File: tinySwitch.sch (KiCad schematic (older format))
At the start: 14 parts, among them J0 Conn_01x02, J1 Conn_01x03, J2 Conn_01x02, J3 Conn_01x02, J4 Conn_01x02, K1 1 Channel Relay, SW1 Power Button, U1 Digispark Tiny85

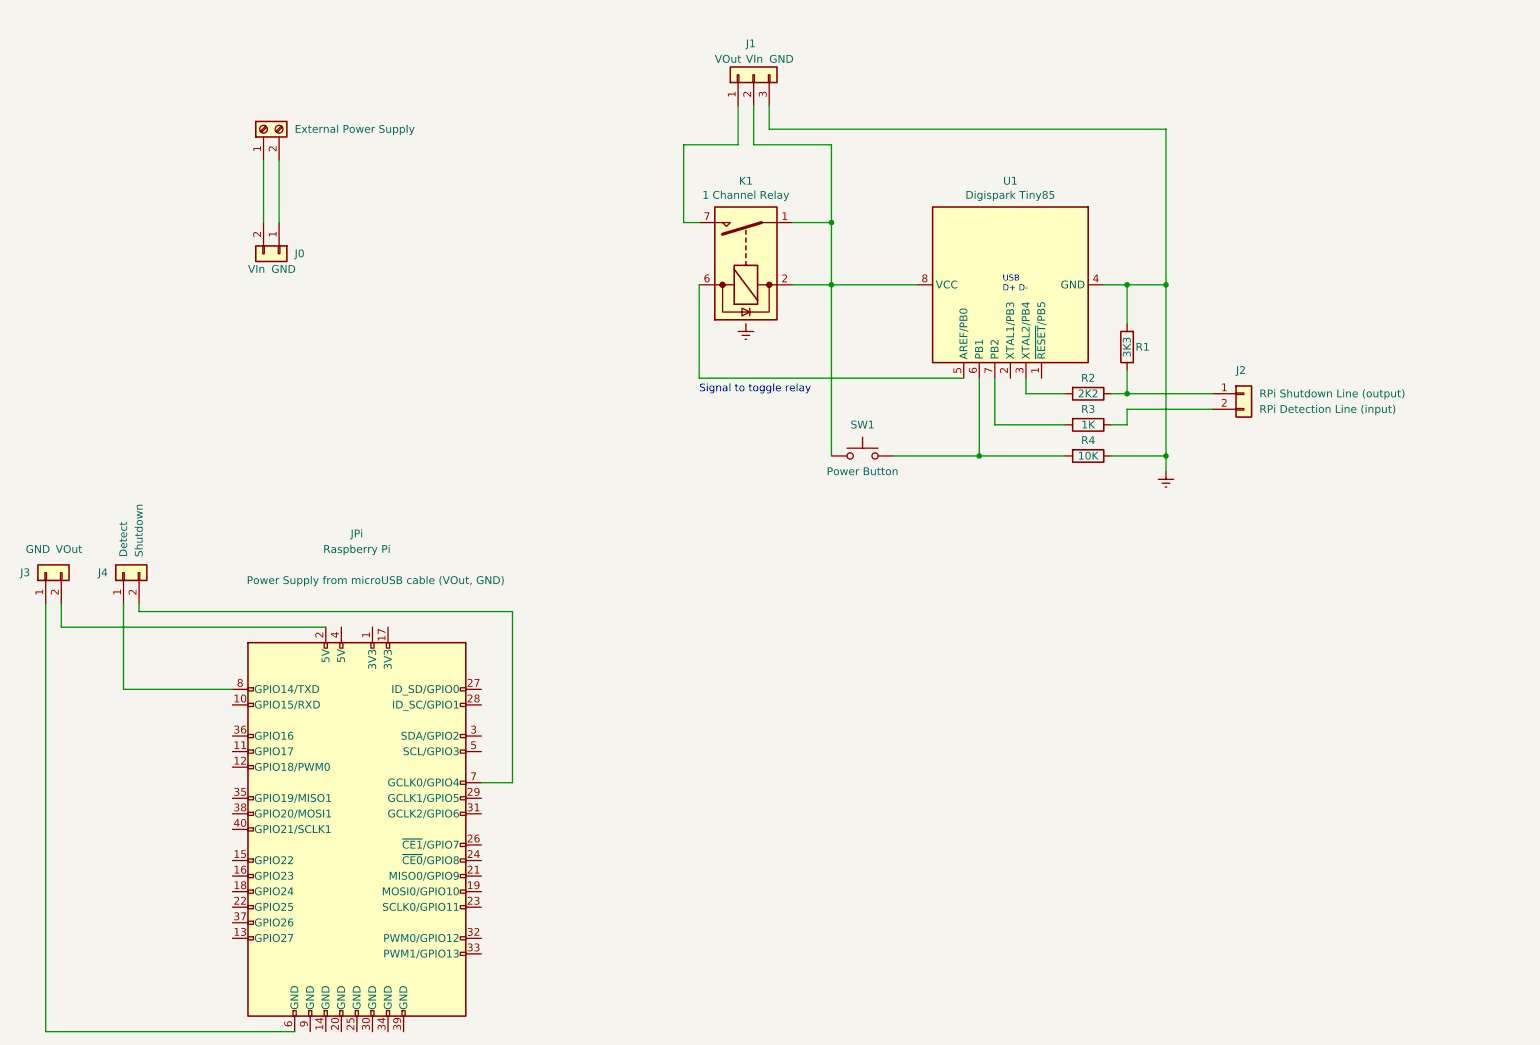
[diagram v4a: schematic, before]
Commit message: GPIO 23-22 for I/O
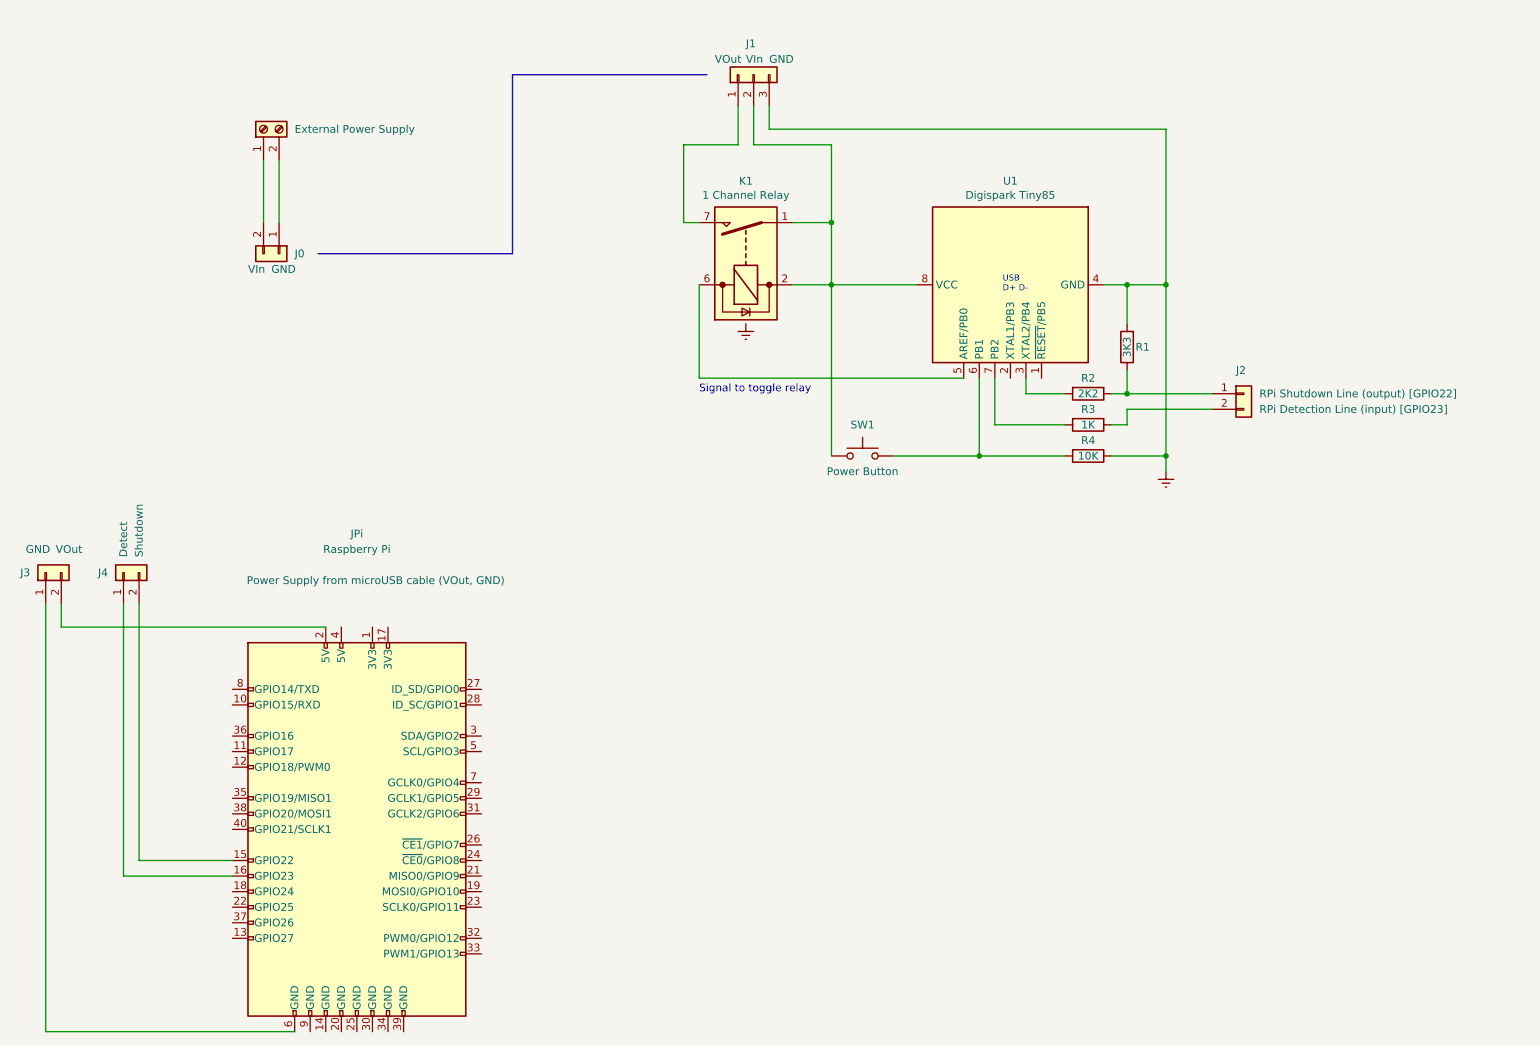
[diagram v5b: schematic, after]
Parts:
- J2: Input RPi Detection Line (input) -> RPi Detection Line (input) [GPIO23]; Output RPi Shutdown Line (output) -> RPi Shutdown Line (output) [GPIO22]
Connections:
- net at JPi.15 (GPIO22): now also J4.2 (Pin_2)
- net at JPi.16 (GPIO23): now also J4.1 (Pin_1)
- net at JPi.7 (GCLK0/GPIO4): no longer J4.2 (Pin_2)
- net at JPi.8 (GPIO14/TXD): no longer J4.1 (Pin_1)
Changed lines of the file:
@@
 Sheet 1 1
 Title "tinySwitch"
-Date "2020-11-26"
-Rev "1.1"
+Date "2020-12-06"
+Rev "1.2"
 Comp "Ben"
 Comment1 ""
@@
 F 2 "" H 9200 3250 50  0001 C CNN
 F 3 "~" H 9200 3250 50  0001 C CNN
-F 4 "RPi Shutdown Line (output)" H 9300 3250 50  0000 L CNN "Output"
-F 5 "RPi Detection Line (input) " H 9300 3150 50  0000 L CNN "Input"
+F 4 "RPi Shutdown Line (output)  [GPIO22]" H 9300 3250 50  0000 L CNN "Output"
+F 5 "RPi Detection Line (input)    [GPIO23]" H 9300 3150 50  0000 L CNN "Input"
 	1    9200 3250
 	1    0    0    -1
@@
 	0    -1   -1   0
 $EndComp
-Wire Wire Line
-	2700 5150 2000 5150
-Wire Wire Line
-	2000 5150 2000 4600
-Wire Wire Line
-	4300 5750 4500 5750
-Wire Wire Line
-	4500 5750 4500 4650
-Wire Wire Line
-	4500 4650 2100 4650
-Wire Wire Line
-	2100 4650 2100 4600
 $Comp
 L Connector_Generic:Conn_01x02 J0
@@
 Text Notes 5700 3250 0    49   ~ 0
 Signal to toggle relay
+Wire Wire Line
+	2000 6350 2700 6350
+Wire Wire Line
+	2000 4600 2000 6350
+Wire Wire Line
+	2100 4600 2100 6250
+Wire Wire Line
+	2100 6250 2700 6250
+Wire Bus Line
+	3250 2350 4500 2350
+Wire Bus Line
+	4500 2350 4500 1200
+Wire Bus Line
+	4500 1200 5750 1200
 $EndSCHEMATC
